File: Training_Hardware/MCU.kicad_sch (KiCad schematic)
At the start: 2 parts, among them J1 RJ45_LED_Shielded, U1 Teensy4.1_DEV-16771

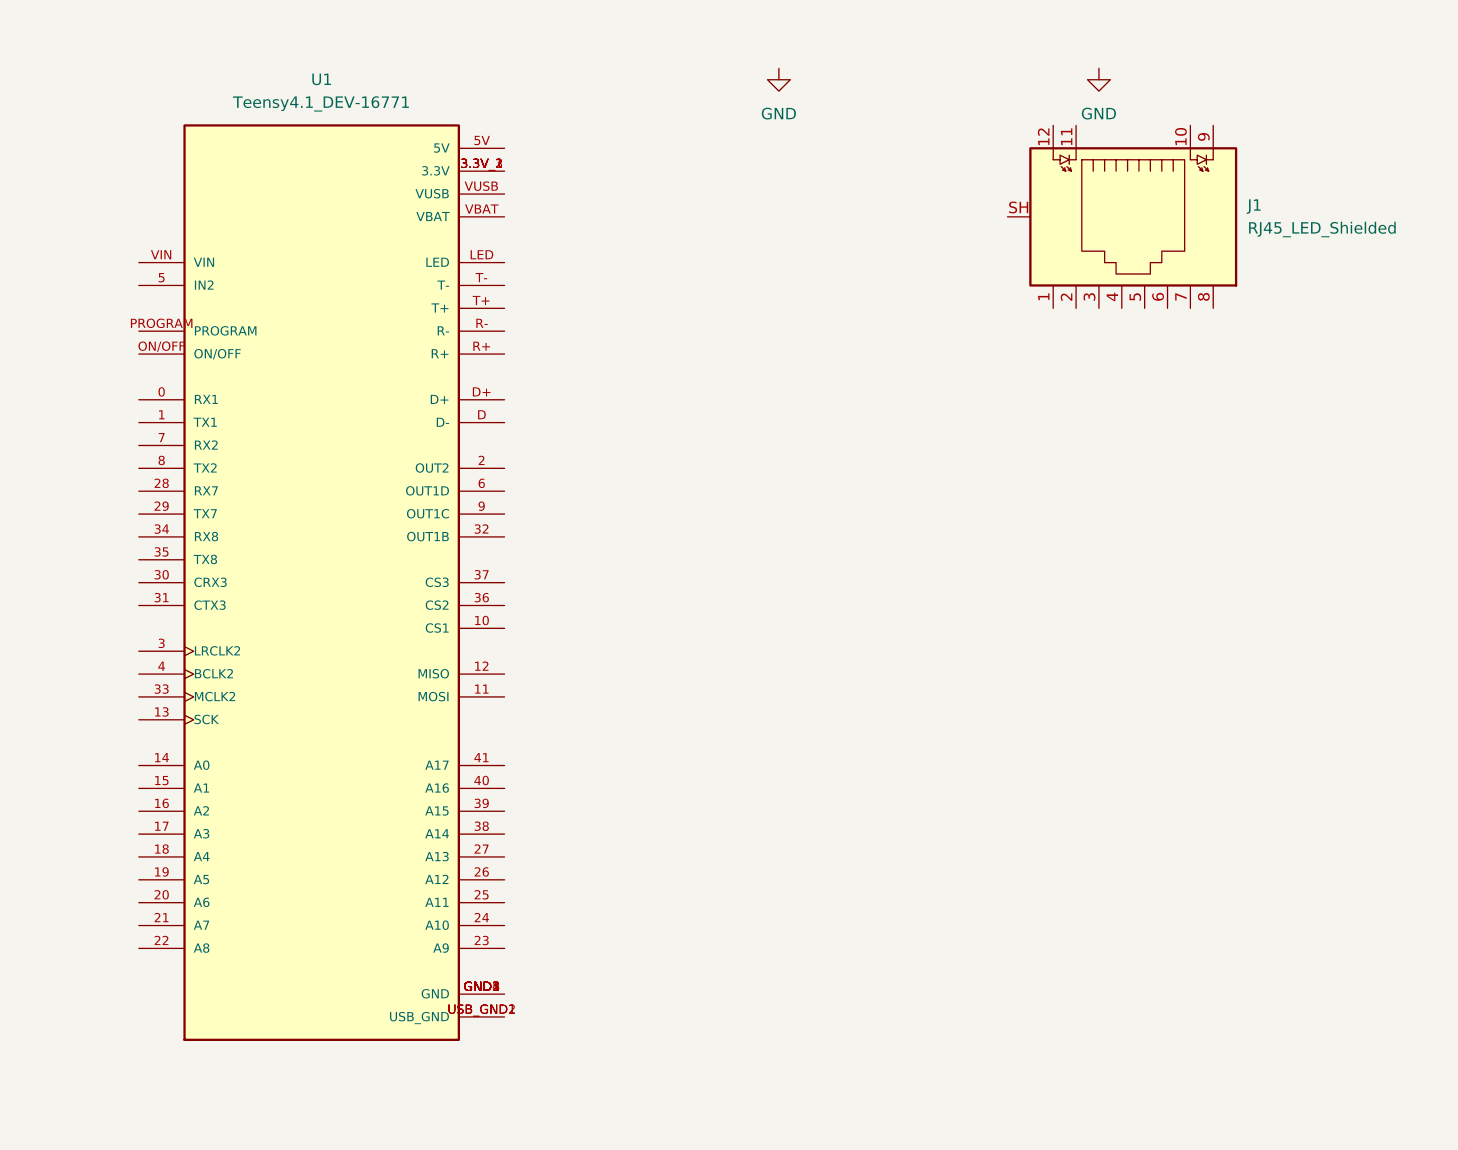
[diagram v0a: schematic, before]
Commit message: Add Ethernet
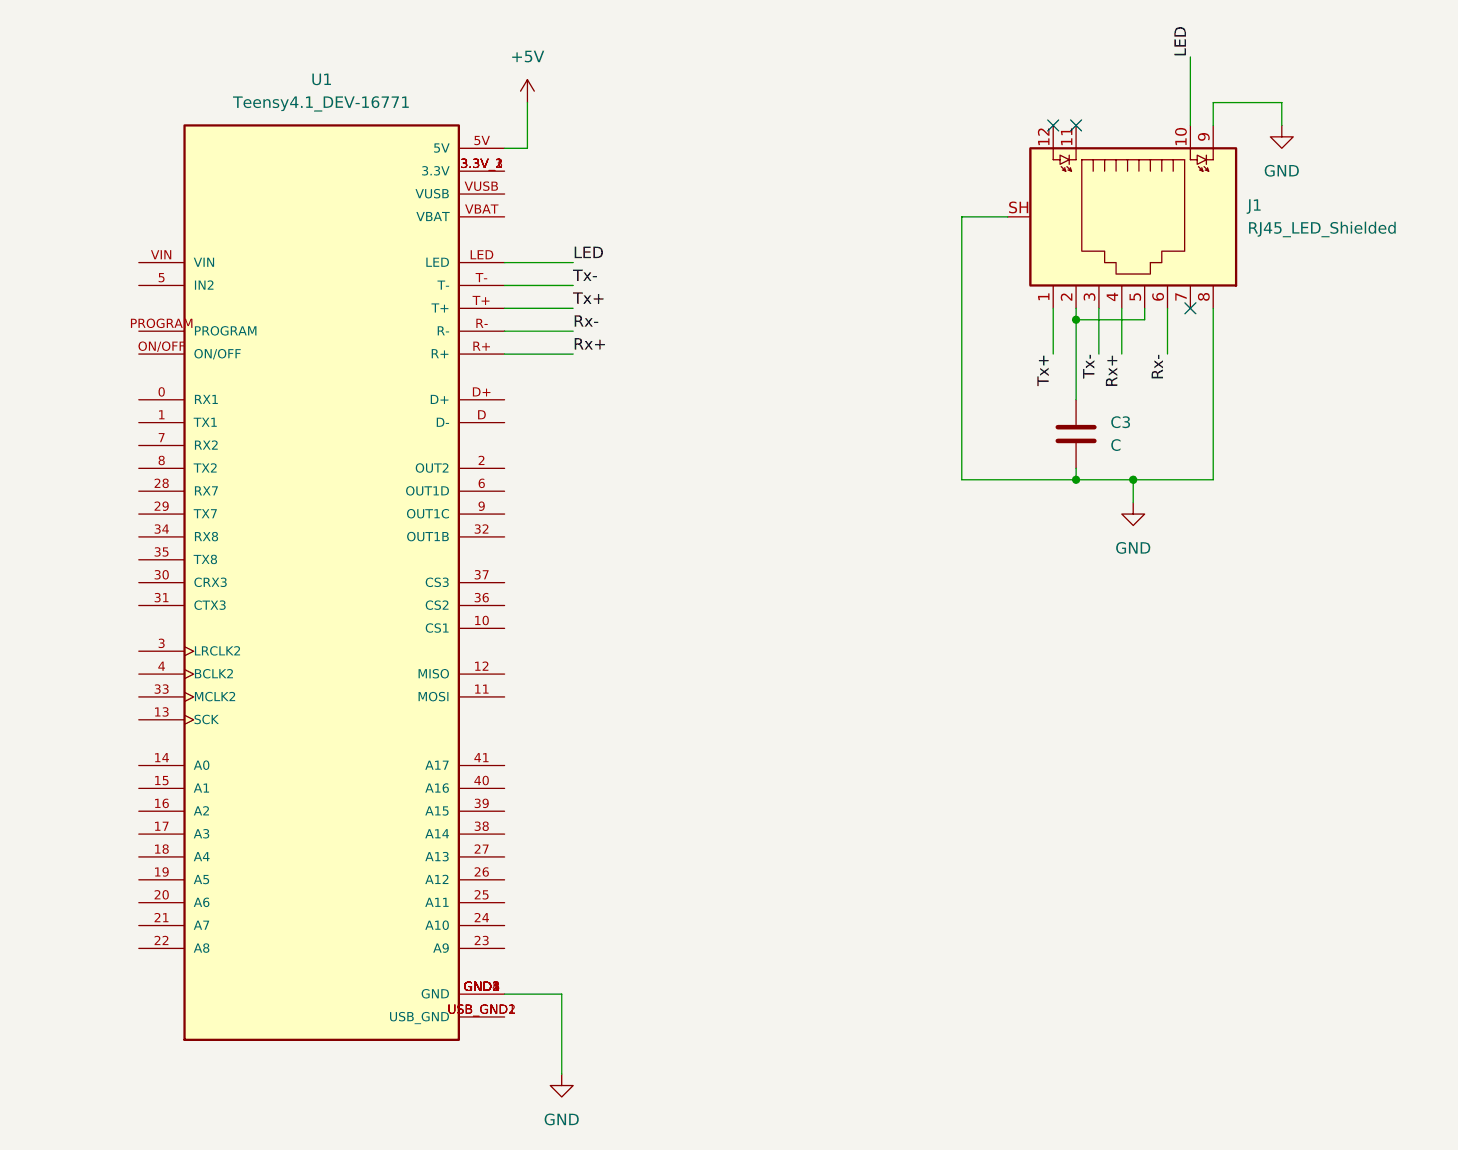
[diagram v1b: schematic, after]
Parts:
- added C3: C, symbol Device:C
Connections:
- net GND: now also J1.8, J1.9, J1.SH, U1.GND1 (GND), U1.GND2 (GND), U1.GND3 (GND), U1.GND4 (GND), U1.GND5 (GND), C3.2
- net Tx+: now reaches J1.1
- net Tx+: now also U1.T+
- net LED: now reaches J1.10
- net LED: now also U1.LED
- net at J1.2: now also J1.5, C3.1
- net Tx-: now reaches J1.3
- net Tx-: now also U1.T-
- net Rx+: now reaches J1.4
- net Rx+: now also U1.R+
- net Rx-: now reaches J1.6
- net Rx-: now also U1.R-
- net +5V: now reaches U1.5V
- no-connect marks 0 -> 3

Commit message: Finish Schematic
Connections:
- net STBY: now reaches U1.2 (OUT2)
- net CTX 1: now reaches U1.22 (A8)
- net CRX 1: now reaches U1.23 (A9)
- net +3V3: now reaches U1.3.3V_1 (3.3V), U1.3.3V_2 (3.3V), U1.3.3V_3 (3.3V)
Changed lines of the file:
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@@
+	(wire
+		(pts
+			(xy 165.1 53.34) (xy 156.21 53.34)
+		)
+		(stroke
+			(width 0)
+			(type default)
+		)
+	)
 	(wire
 		(pts
@@
 	(wire
 		(pts
+			(xy 156.21 139.7) (xy 160.02 139.7)
+		)
+		(stroke
+			(width 0)
+			(type default)
+		)
+	)
+	(wire
+		(pts
 			(xy 229.87 68.58) (xy 229.87 73.66)
 		)
@@
 	(wire
 		(pts
+			(xy 156.21 86.36) (xy 162.56 86.36)
+		)
+		(stroke
+			(width 0)
+			(type default)
+		)
+	)
+	(wire
+		(pts
 			(xy 158.75 50.8) (xy 158.75 45.72)
 		)
@@
 	(wire
 		(pts
+			(xy 110.49 139.7) (xy 115.57 139.7)
+		)
+		(stroke
+			(width 0)
+			(type default)
+		)
+	)
+	(wire
+		(pts
 			(xy 217.17 68.58) (xy 217.17 73.66)
 		)
@@
 		(pts
 			(xy 222.25 68.58) (xy 222.25 73.66)
+		)
+		(stroke
+			(width 0)
+			(type default)
+		)
+	)
+	(wire
+		(pts
+			(xy 165.1 45.72) (xy 165.1 53.34)
 		)
 		(stroke
@@
 			)
 			(justify left bottom)
+		)
+	)
+	(hierarchical_label "CRX 1"
+		(shape input)
+		(at 160.02 139.7 0)
+		(effects
+			(font
+				(size 1.27 1.27)
+			)
+			(justify left)
+		)
+	)
+	(hierarchical_label "STBY"
+		(shape output)
+		(at 162.56 86.36 0)
+		(effects
+			(font
+				(size 1.27 1.27)
+			)
+			(justify left)
+		)
+	)
+	(hierarchical_label "CTX 1"
+		(shape output)
+		(at 110.49 139.7 180)
+		(effects
+			(font
+				(size 1.27 1.27)
+			)
+			(justify right)
 		)
 	)
@@
 					(unit 1)
 				)
+			)
+		)
+	)
+	(symbol
+		(lib_id "power:+3V3")
+		(at 165.1 45.72 0)
+		(unit 1)
+		(exclude_from_sim no)
+		(in_bom yes)
+		(on_board yes)
+		(dnp no)
+		(fields_autoplaced yes)
+		(property "Reference" "#PWR016"
+			(at 165.1 49.53 0)
+			(effects
+				(font
+					(size 1.27 1.27)
+				)
+				(hide yes)
+			)
+		)
+		(property "Value" "+3V3"
+			(at 165.1 40.64 0)
+			(effects
+				(font
+					(size 1.27 1.27)
+				)
+			)
+		)
+		(property "Footprint" ""
+			(at 165.1 45.72 0)
+			(effects
+				(font
+					(size 1.27 1.27)
+				)
+				(hide yes)
+			)
+		)
+		(property "Datasheet" ""
+			(at 165.1 45.72 0)
+			(effects
+				(font
+					(size 1.27 1.27)
+				)
+				(hide yes)
+			)
+		)
+		(property "Description" "Power symbol creates a global label with name \"+3V3\""
+			(at 165.1 45.72 0)
+			(effects
+				(font
+					(size 1.27 1.27)
+				)
+				(hide yes)
+			)
+		)
+		(pin "1"
+		)
+		(instances
+			(project ""
+				(path "/b0d5b3f6-1860-46b8-b850-3c3e521e5123/4e418afb-b30e-4314-af6c-a7c671982343"
+					(reference "#PWR016")
+					(unit 1)
+				)
